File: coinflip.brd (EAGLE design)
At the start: 38.1 x 38.1 mm, 17 parts, among them IC1 LM358N, IC2 4027N, T1 2N3904, T2 2N3904

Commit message: Version 2.0 commit
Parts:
- added C4: 10uF, rcl:C025-024X044
- moved R5 5.08 mm to (11.4, 29.2)
- moved IC2 2.54 mm to (31.8, 11.4)
- moved R1 2.54 mm to (6.35, 29.2)
- moved R2 2.54 mm to (8.89, 29.2)
- turned LED1 to 0 degrees
- turned LED2 to 0 degrees
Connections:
- net GND: now also C4.2
- net VDD: now also C4.1
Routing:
- net GND: track 74.1 -> 0.00 mm
- net N$10: track 32.1 -> 24.2 mm
- net N$6: track 31.7 -> 37.7 mm
- net N$8: track 8.72 -> 11.8 mm
- net N$13: track 8.51 -> 11.3 mm
- net VDD: track 78.8 -> 81.4 mm
- net N$4: track 20.1 -> 22.6 mm, vias 0 -> 2
- net N$11: track 16.6 -> 14.4 mm, vias 1 -> 2
- net N$14: track 7.40 -> 5.61 mm
- net N$3: track 12.0 -> 10.5 mm
- net N$5: track 10.6 -> 11.7 mm, vias 0 -> 2
- net N$9: track 7.40 -> 6.35 mm
- added copper zone on layer 16, net GND
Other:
- board text added: "Coin Flip v2"
- board text added: "FLIP"
- board text added: "HEADS"
- board text added: "TAILS"
- board text removed: "Heads"
- board text removed: "Tails"

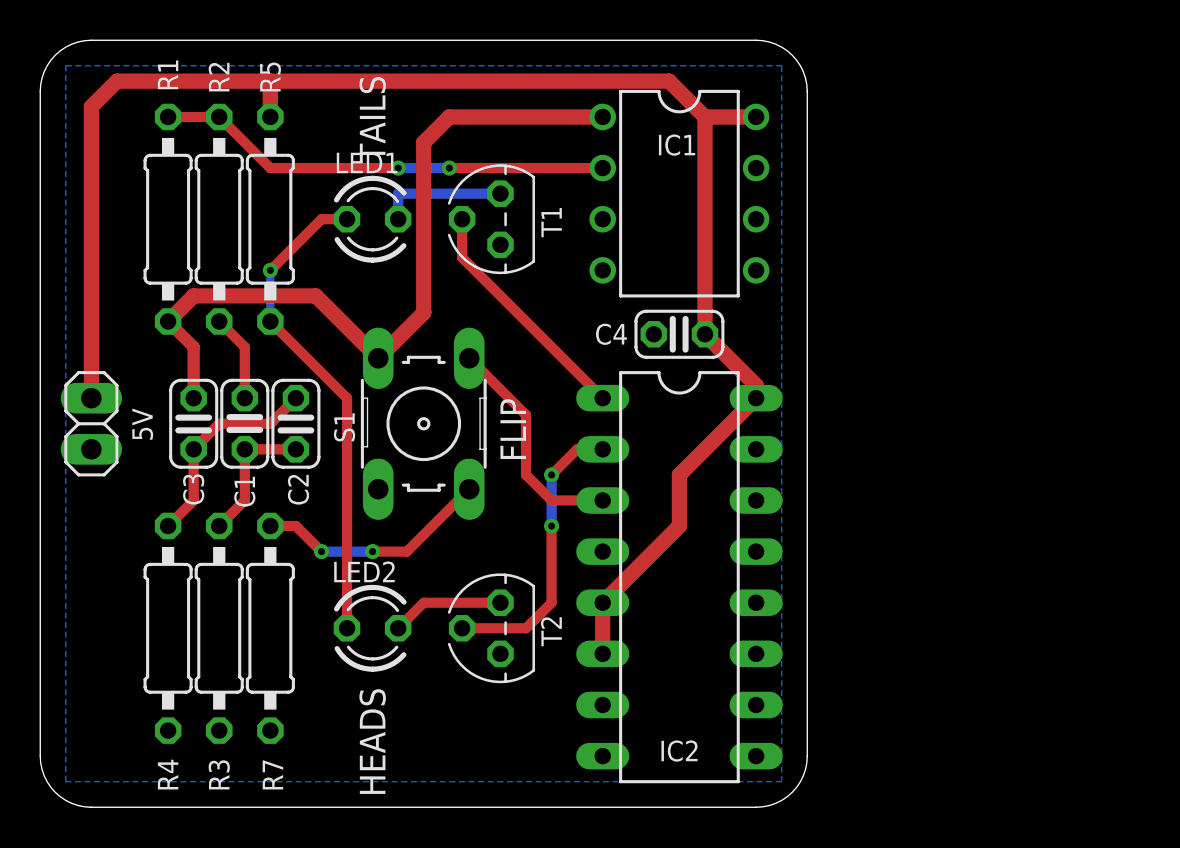
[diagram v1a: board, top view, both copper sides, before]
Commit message: Updated to v3.0: redesigned oscillator, new board layout
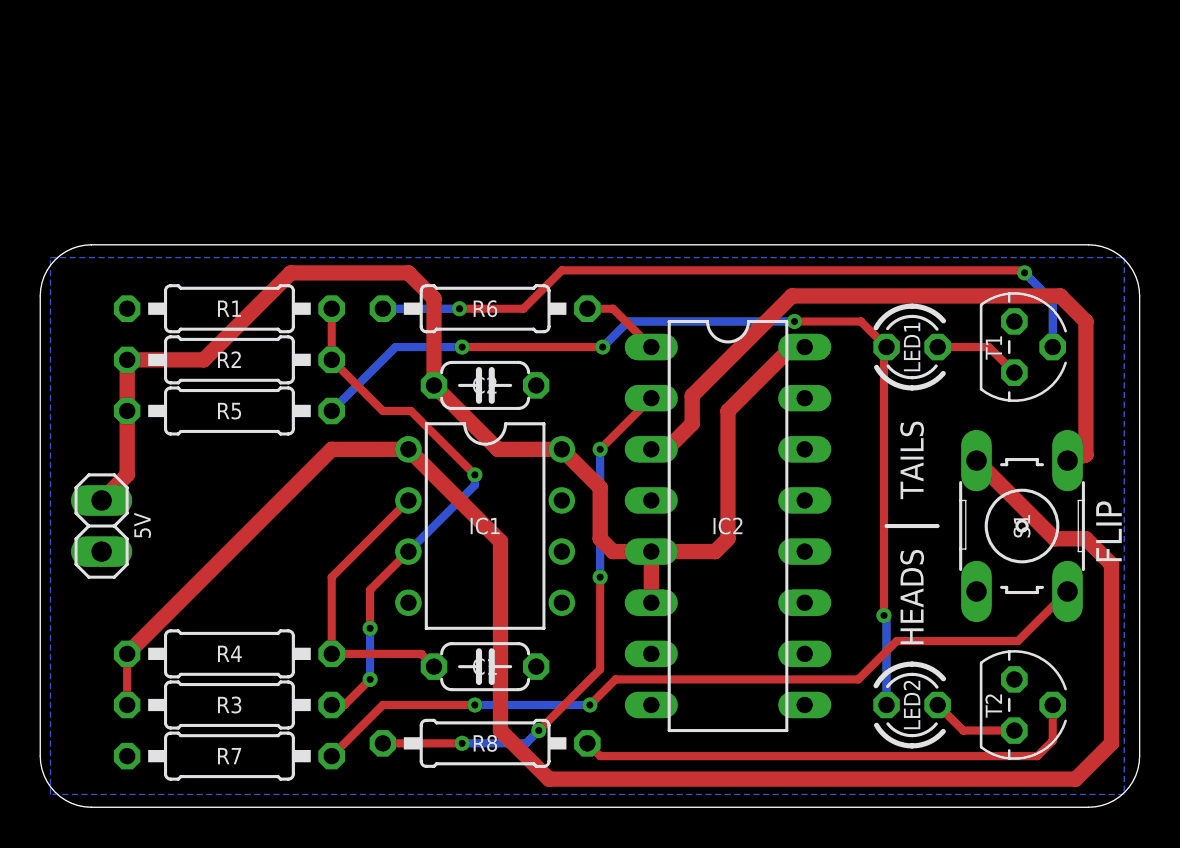
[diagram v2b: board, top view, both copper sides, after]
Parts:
- removed C3: 4.7nF, rcl:C025-024X044
- removed C4: 10uF, rcl:C025-024X044
- added R6, R8: 1k, resistor:0207/10
- C1: value 4.7nF -> 100pF; device rcl:C025-024X044 -> resistor:C050-024X044
- C2: value 4.7nF -> 10uF; device rcl:C025-024X044 -> resistor:C050-024X044
- IC1: value LM358N -> LM393N
- LED1, LED2: device led:LED3MM -> led_nofill:LED3MM
- R1: value 33k -> 20k
- R2, R3: value 1k -> 20k
- R4: value 1k -> 6.8k
- moved S1 30.1 mm to (48.8, 14.0)
- moved LED1 27.5 mm to (43.3, 22.9)
- moved LED2 27.1 mm to (43.3, 5.08)
- moved T1 26.3 mm to (48.4, 22.9), turned to 270 degrees
- moved T2 25.8 mm to (48.4, 5.08), turned to 270 degrees
- moved IC1 19.1 mm to (22.1, 14.0)
- moved C1 17.0 mm to (22.1, 6.99), turned to 0 degrees
- moved R5 9.74 mm to (9.40, 19.7), turned to 180 degrees
- moved C2 9.59 mm to (22.1, 21.0), turned to 0 degrees
- moved R2 7.00 mm to (9.40, 22.2), turned to 180 degrees
- moved R7 6.67 mm to (9.40, 2.54), turned to 0 degrees
- moved R1 5.39 mm to (9.40, 24.8), turned to 0 degrees
- moved JP1 5.11 mm to (3.05, 14.0)
- moved R3 3.84 mm to (9.40, 5.08), turned to 0 degrees
- moved IC2 3.50 mm to (34.2, 14.0)
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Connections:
- removed net N$11: IC2.2, T2.2
- new net N$7: IC2.2, R8.2
- net GND: now also C1.2, C2.2, R1.1; no longer C4.2, IC1.3, R3.1, R4.1
- net N$1: now also IC1.1, R3.1, R4.1, S1.3; no longer C1.2, R2.1
- net N$2: now also IC1.3, R1.2, R2.1; no longer C1.1, C2.2
- net N$3: now also C1.1, IC1.2; no longer C2.1, C3.2
- net N$4: now also IC2.1, R6.2; no longer IC1.2, R1.1, R2.2
- net N$6: now also R6.1, T1.2; no longer C3.1, IC1.1, R1.2, S1.3
- net N$8: now also R8.1, T2.2; no longer IC2.1, T1.2
- net VDD: now also C2.1, R2.2; no longer C4.1
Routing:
- net N$1: track 4.34 -> 86.4 mm
- net N$5: track 11.7 -> 39.9 mm
- net N$7: track 0.00 -> 26.8 mm, vias 0 -> 4
- net N$10: track 24.2 -> 47.9 mm, vias 1 -> 4
- net N$13: track 11.3 -> 33.7 mm
- net N$2: track 6.88 -> 26.8 mm, vias 0 -> 3
- net N$4: track 22.6 -> 3.96 mm, vias 2 -> 0
- net VDD: track 81.4 -> 63.2 mm
- net N$11: track 14.4 -> 0.00 mm, vias 2 -> 0
- net N$8: track 11.8 -> 25.5 mm
- net N$3: track 10.5 -> 14.5 mm
- net N$9: track 6.35 -> 4.34 mm
- net N$14: track 5.61 -> 4.34 mm
- net N$6: track 37.7 -> 37.1 mm, vias 0 -> 2
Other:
- board size 38.1 x 38.1 mm -> 54.6 x 27.9 mm
- board text added: "Coin Flip v3.0"
- board text removed: "Coin Flip v2"

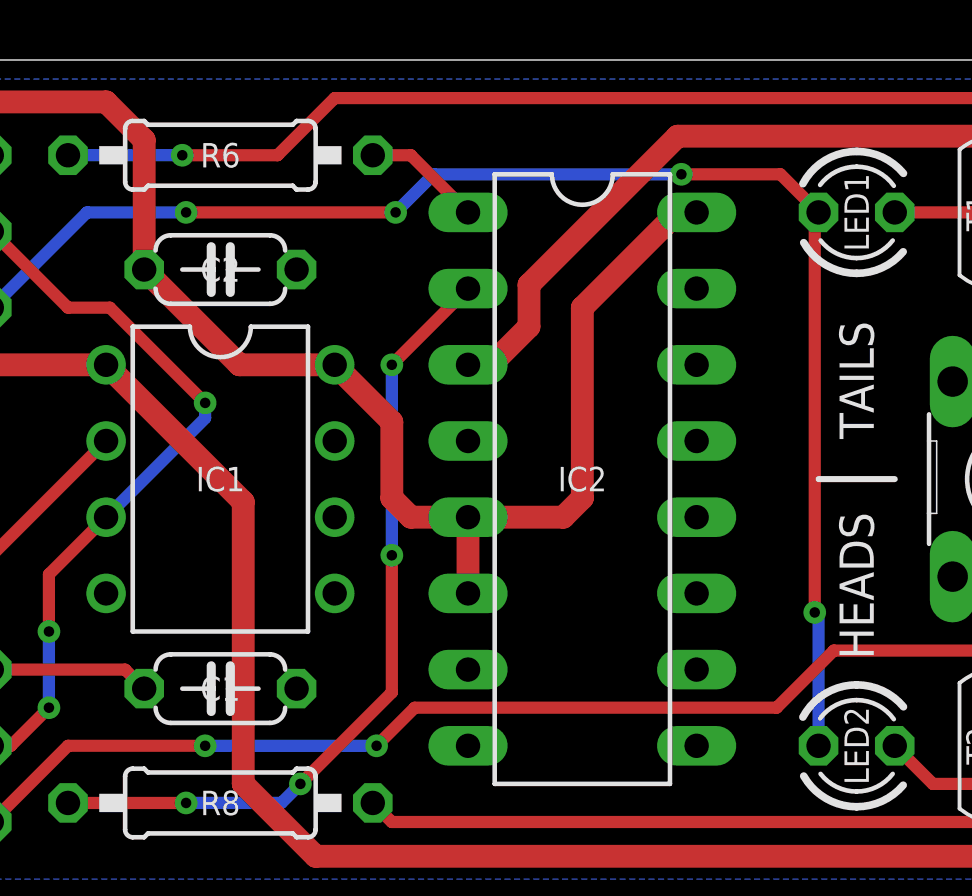
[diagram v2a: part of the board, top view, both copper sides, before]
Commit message: Version 3.1, added BOM and adjusted routing and silkscreen
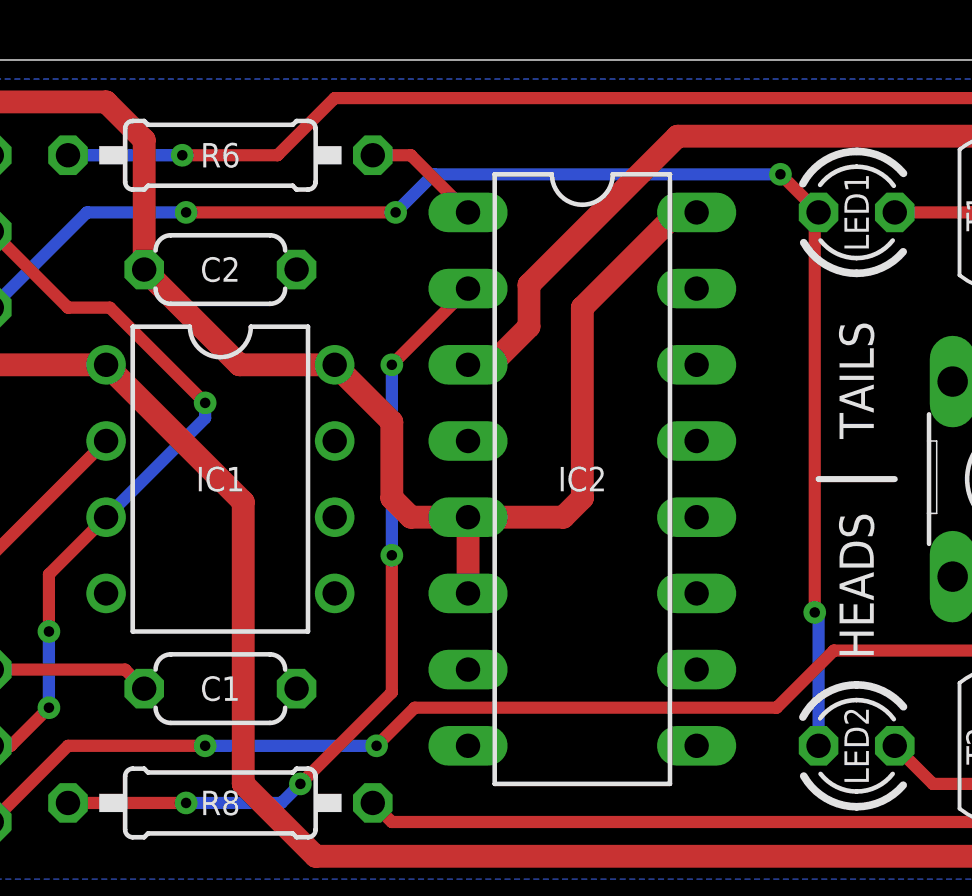
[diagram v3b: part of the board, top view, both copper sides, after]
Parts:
- C1: value 100pF -> 10nF; device resistor:C050-024X044 -> resistor_nofill:C050-024X044
- C2: device resistor:C050-024X044 -> resistor_nofill:C050-024X044
- R4: value 6.8k -> 4.7k
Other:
- board text added: "Coin Flip v3.1"
- board text removed: "Coin Flip v3.0"
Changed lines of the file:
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@@
 <text x="5.08" y="13.97" size="0.8128" layer="25" rot="R90" align="center">5V</text>
 <text x="53.721" y="12.065" size="1.27" layer="21" rot="R90" grouprefs="BUTTON">FLIP</text>
-<text x="33.528" y="9.652" size="1.27" layer="22" rot="MR90">Coin Flip v3.0</text>
+<text x="33.528" y="9.652" size="1.27" layer="22" rot="MR90">Coin Flip v3.1</text>
 <wire x1="52.07" y1="0" x2="2.54" y2="0" width="0" layer="20"/>
 <wire x1="2.54" y1="0" x2="0" y2="2.54" width="0" layer="20" curve="-90"/>
@@
 <attribute name="VALUE" x="7.1374" y="4.445" size="1.27" layer="27" ratio="10"/>
 </element>
-<element name="R4" library="resistor" library_urn="urn:adsk.eagle:library:348" package="0207/10" package3d_urn="urn:adsk.eagle:package:23491/2" value="6.8k" x="9.398" y="7.62" smashed="yes">
+<element name="R4" library="resistor" library_urn="urn:adsk.eagle:library:348" package="0207/10" package3d_urn="urn:adsk.eagle:package:23491/2" value="4.7k" x="9.398" y="7.62" smashed="yes">
 <attribute name="NAME" x="9.398" y="7.62" size="0.8128" layer="25" ratio="10" align="center"/>
 <attribute name="VALUE" x="7.1374" y="6.985" size="1.27" layer="27" ratio="10"/>
@@
 <attribute name="VALUE" x="21.463" y="17.526" size="1.27" layer="27" ratio="10" rot="R270"/>
 </element>
-<element name="C1" library="resistor" library_urn="urn:adsk.eagle:library:348" package="C050-024X044" package3d_urn="urn:adsk.eagle:package:23643/1" value="100pF" x="22.098" y="6.985" smashed="yes">
+<element name="C1" library="resistor_nofill" package="C050-024X044" package3d_urn="urn:adsk.eagle:package:23643/1" value="10nF" x="22.098" y="6.985" smashed="yes">
 <attribute name="NAME" x="22.098" y="6.985" size="0.8128" layer="25" ratio="10" align="center"/>
 <attribute name="VALUE" x="19.939" y="4.318" size="1.27" layer="27" ratio="10"/>
@@
 <attribute name="VALUE" x="24.3586" y="3.81" size="1.27" layer="27" ratio="10" rot="R180"/>
 </element>
-<element name="C2" library="resistor" library_urn="urn:adsk.eagle:library:348" package="C050-024X044" package3d_urn="urn:adsk.eagle:package:23643/1" value="10uF" x="22.098" y="20.955" smashed="yes">
+<element name="C2" library="resistor_nofill" package="C050-024X044" package3d_urn="urn:adsk.eagle:package:23643/1" value="10uF" x="22.098" y="20.955" smashed="yes">
 <attribute name="NAME" x="22.098" y="20.955" size="0.8128" layer="25" ratio="10" align="center"/>
 <attribute name="VALUE" x="19.939" y="18.288" size="1.27" layer="27" ratio="10"/>
@@
 <via x="27.94" y="22.86" extent="1-16" drill="0.35"/>
 <wire x1="27.94" y1="22.86" x2="29.21" y2="24.13" width="0.4064" layer="16"/>
-<wire x1="29.21" y1="24.13" x2="37.465" y2="24.13" width="0.4064" layer="16"/>
-<via x="37.465" y="24.13" extent="1-16" drill="0.35"/>
 <wire x1="42.037" y1="5.08" x2="42.037" y2="9.525" width="0.4064" layer="16"/>
 <wire x1="42.037" y1="9.525" x2="41.91" y2="9.525" width="0.4064" layer="16"/>
@@
 <wire x1="41.91" y1="9.525" x2="41.91" y2="22.733" width="0.4064" layer="1"/>
 <wire x1="41.91" y1="22.733" x2="42.037" y2="22.86" width="0.4064" layer="1"/>
-<wire x1="37.465" y1="24.13" x2="40.767" y2="24.13" width="0.4064" layer="1"/>
 <wire x1="40.767" y1="24.13" x2="42.037" y2="22.86" width="0.4064" layer="1"/>
+<via x="40.767" y="24.13" extent="1-16" drill="0.35"/>
+<wire x1="29.21" y1="24.13" x2="40.767" y2="24.13" width="0.4064" layer="16"/>
 </signal>
 <signal name="N$14">
